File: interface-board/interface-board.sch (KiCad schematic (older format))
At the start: 21 parts, among them J1 HECS, J10 AUX, J11 UART, J12 NTC1, J13 NTC1, J16 Conn_01x23, J2 CASEFAN1, J3 CASEFAN2, J4 Bender-LV, J6 HV+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

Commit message: Getting there with layout of big board...
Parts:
- removed C2: 470uF, Capacitor_THT:CP_Radial_D10.0mm_P5.00mm, symbol Device:C
- removed F4: 20A, Fuse:Fuseholder_Cylinder-5x20mm_Schurter_0031_8201_Horizontal_Open, symbol Device:Fuse
- removed JP5: SolderJumper_2_Open, Jumper:SolderJumper-2_P1.3mm_Open_RoundedPad1.0x1.5mm, symbol Jumper:SolderJumper_2_Open
- removed JP6, JP7: SolderJumper_2_Bridged, Jumper:SolderJumper-2_P1.3mm_Bridged_RoundedPad1.0x1.5mm, symbol Jumper:SolderJumper_2_Bridged
- added F1: 2A, CustomFootprints:Fuseholder_Cylinder-5x20mm_Schurter_0031_8201_Horizontal_Open_3d, symbol Device:Fuse
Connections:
- wire segments 107 -> 104
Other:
- note added: "Return from safety loop"
- note added: "change to open jumpers"
- note removed: "Fuses?"

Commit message: Interface-board largely routed
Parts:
- removed J10: AUX, Connector_Wago:Wago_734-134_1x04_P3.50mm_Vertical, symbol Connector_Generic:Conn_01x02
- removed JP2, JP3: Jumper, Jumper:SolderJumper-2_P1.3mm_Open_RoundedPad1.0x1.5mm, symbol Jumper:SolderJumper_2_Open
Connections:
- net labels added: SCL, SDA
- wire segments 104 -> 100
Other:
- moved on the sheet: F1

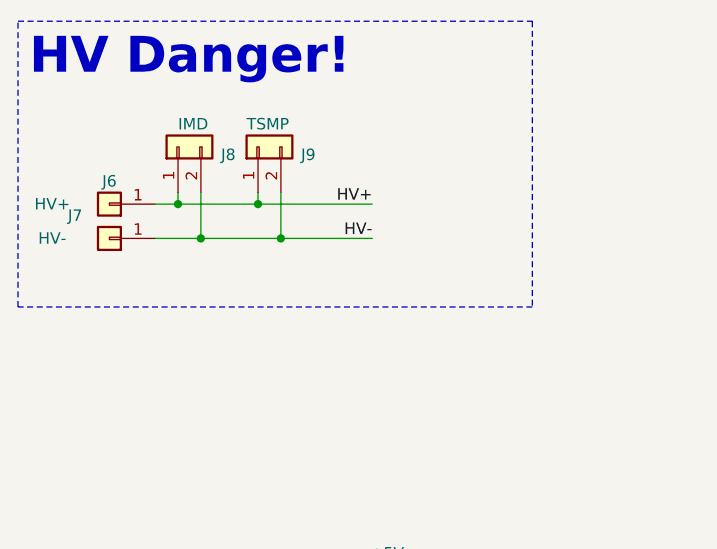
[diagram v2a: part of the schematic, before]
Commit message: Fully routed, added blinky DC/DC, added silkscreen labels, bumped 5V traces up to 0.025"
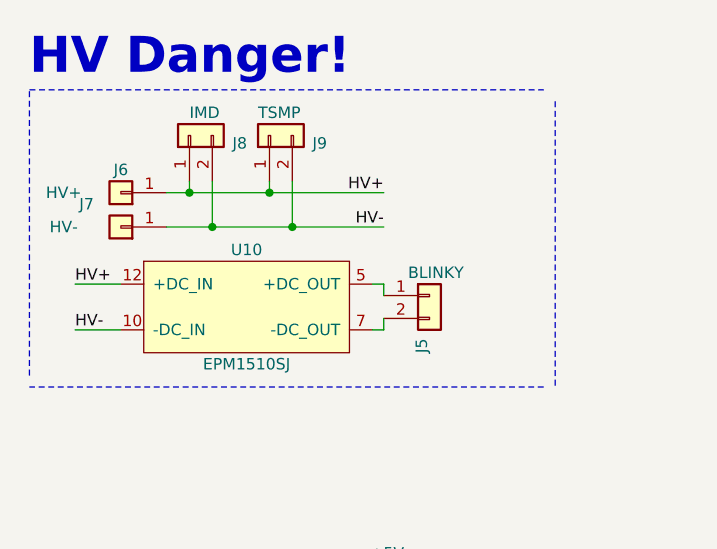
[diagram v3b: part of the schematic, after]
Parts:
- added J5: BLINKY, Connector_Phoenix_MC_HighVoltage:PhoenixContact_MCV_1,5_2-G-5.08_1x02_P5.08mm_Vertical, symbol Connector_Generic:Conn_01x02
- added U10: EPM1510SJ, CustomFootprints:EPM1510SJ, symbol CUSTOM_IC:EPM1510SJ
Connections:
- net HV+: now also U10.12 (+DC_IN)
- net HV-: now also U10.10 (-DC_IN)
- new net: J5.1 (Pin_1), U10.5 (+DC_OUT)
- new net: J5.2 (Pin_2), U10.7 (-DC_OUT)
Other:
- moved on the sheet: J6, J7, J8, J9
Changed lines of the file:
@@
 Comment4 ""
 $EndDescr
-Text Label 2100 1350 2    50   ~ 0
+Text Label 2150 1300 2    50   ~ 0
 HV+
-Text Label 2100 1500 2    50   ~ 0
+Text Label 2150 1450 2    50   ~ 0
 HV-
 Text Label 1350 6150 2    50   ~ 0
@@
 L Connector_Generic:Conn_01x01 J7
 U 1 1 5C7C388D
-P 950 1500
-F 0 "J7" H 1100 1400 50  0000 C CNN
-F 1 "HV-" H 1200 1500 50  0000 C CNN
-F 2 "MountingHole:MountingHole_4.3mm_M4_Pad_Via" H 950 1500 50  0001 C CNN
-F 3 "~" H 950 1500 50  0001 C CNN
-	1    950  1500
+P 1000 1450
+F 0 "J7" H 1150 1350 50  0000 C CNN
+F 1 "HV-" H 1250 1450 50  0000 C CNN
+F 2 "MountingHole:MountingHole_4.3mm_M4_Pad_Via" H 1000 1450 50  0001 C CNN
+F 3 "~" H 1000 1450 50  0001 C CNN
+	1    1000 1450
 	-1   0    0    1
 $EndComp
@@
 L Connector_Generic:Conn_01x01 J6
 U 1 1 5C83C6D2
-P 950 1350
-F 0 "J6" H 950 1250 50  0000 C CNN
-F 1 "HV+" H 1200 1350 50  0000 C CNN
-F 2 "MountingHole:MountingHole_4.3mm_M4_Pad_Via" H 950 1350 50  0001 C CNN
-F 3 "~" H 950 1350 50  0001 C CNN
-	1    950  1350
+P 1000 1300
+F 0 "J6" H 1000 1200 50  0000 C CNN
+F 1 "HV+" H 1250 1300 50  0000 C CNN
+F 2 "MountingHole:MountingHole_4.3mm_M4_Pad_Via" H 1000 1300 50  0001 C CNN
+F 3 "~" H 1000 1300 50  0001 C CNN
+	1    1000 1300
 	-1   0    0    1
 $EndComp
@@
 L Connector_Generic:Conn_01x02 J8
 U 1 1 5C871653
-P 1250 1100
-F 0 "J8" V 1216 912 50  0000 R CNN
-F 1 "IMD" V 1350 1100 50  0000 R CNN
-F 2 "Connector_Phoenix_MC_HighVoltage:PhoenixContact_MCV_1,5_2-G-5.08_1x02_P5.08mm_Vertical" H 1250 1100 50  0001 C CNN
-F 3 "~" H 1250 1100 50  0001 C CNN
-	1    1250 1100
+P 1300 1050
+F 0 "J8" V 1266 862 50  0000 R CNN
+F 1 "IMD" V 1400 1050 50  0000 R CNN
+F 2 "Connector_Phoenix_MC_HighVoltage:PhoenixContact_MCV_1,5_2-G-5.08_1x02_P5.08mm_Vertical" H 1300 1050 50  0001 C CNN
+F 3 "~" H 1300 1050 50  0001 C CNN
+	1    1300 1050
 	0    -1   -1   0
 $EndComp
 Wire Wire Line
-	1150 1350 1250 1350
-Wire Wire Line
-	1250 1300 1250 1350
-Wire Wire Line
-	1350 1300 1350 1500
-Wire Wire Line
-	1350 1500 1150 1500
-Connection ~ 1250 1350
+	1200 1300 1300 1300
+Wire Wire Line
+	1300 1250 1300 1300
+Wire Wire Line
+	1400 1250 1400 1450
+Wire Wire Line
+	1400 1450 1200 1450
+Connection ~ 1300 1300
 $Sheet
 S 4600 1150 1600 900
@@
 L Connector_Generic:Conn_01x02 J9
 U 1 1 5C4C2740
-P 1600 1100
-F 0 "J9" V 1566 912 50  0000 R CNN
-F 1 "TSMP" V 1700 1150 50  0000 R CNN
-F 2 "Connector_Phoenix_MC_HighVoltage:PhoenixContact_MCV_1,5_2-G-5.08_1x02_P5.08mm_Vertical" H 1600 1100 50  0001 C CNN
-F 3 "~" H 1600 1100 50  0001 C CNN
-	1    1600 1100
+P 1650 1050
+F 0 "J9" V 1616 862 50  0000 R CNN
+F 1 "TSMP" V 1750 1100 50  0000 R CNN
+F 2 "Connector_Phoenix_MC_HighVoltage:PhoenixContact_MCV_1,5_2-G-5.08_1x02_P5.08mm_Vertical" H 1650 1050 50  0001 C CNN
+F 3 "~" H 1650 1050 50  0001 C CNN
+	1    1650 1050
 	0    -1   -1   0
 $EndComp
 Wire Wire Line
-	1250 1350 1600 1350
-Wire Wire Line
-	1600 1300 1600 1350
-Connection ~ 1600 1350
-Wire Wire Line
-	1700 1300 1700 1500
-Wire Wire Line
-	1350 1500 1700 1500
-Connection ~ 1350 1500
+	1300 1300 1650 1300
+Wire Wire Line
+	1650 1250 1650 1300
+Connection ~ 1650 1300
+Wire Wire Line
+	1750 1250 1750 1450
+Wire Wire Line
+	1400 1450 1750 1450
+Connection ~ 1400 1450
 Text Label 3850 2550 0    50   ~ 0
 HV+
@@
 Text Label 4300 1350 0    50   ~ 0
 CAN-
-Connection ~ 1700 1500
+Connection ~ 1750 1450
 Text Label 6500 1800 2    50   ~ 0
 TEMP_1
@@
 $EndComp
 Wire Notes Line width 39 rgb(253, 0, 0)
-	550  550  2800 550
+	600  850  2850 850
 Wire Notes Line width 39 rgb(255, 0, 0)
-	2800 550  2800 1800
+	2900 900  2900 2150
 Wire Notes Line width 39 rgb(255, 0, 0)
-	2800 1800 550  1800
+	2850 2150 600  2150
 Wire Notes Line width 39 rgb(255, 0, 0)
-	550  1800 550  550
+	600  2100 600  850
 Text Notes 600  800  0    157  ~ 31
 HV Danger!
 Wire Wire Line
-	1600 1350 2100 1350
-Wire Wire Line
-	1700 1500 2100 1500
+	1650 1300 2150 1300
+Wire Wire Line
+	1750 1450 2150 1450
 $Comp
 L Connector_Generic:Conn_01x23 J16
@@
 Wire Wire Line
 	8850 2450 8950 2450
+$Comp
+L CUSTOM_IC:EPM1510SJ U10
+U 1 1 5C600D22
+P 1550 2000
+F 0 "U10" H 1550 2450 50  0000 C CNN
+F 1 "EPM1510SJ" H 1550 1950 50  0000 C CNN
+F 2 "CustomFootprints:EPM1510SJ" H 1550 2000 50  0001 C CNN
+F 3 "" H 1550 2000 50  0001 C CNN
+	1    1550 2000
+	1    0    0    -1
+$EndComp
+Wire Wire Line
+	1000 1700 800  1700
+Wire Wire Line
+	1000 1900 800  1900
+Text Label 800  1700 0    50   ~ 0
+HV+
+Text Label 800  1900 0    50   ~ 0
+HV-
+$Comp
+L Connector_Generic:Conn_01x02 J5
+U 1 1 5C61B783
+P 2350 1750
+F 0 "J5" V 2316 1562 50  0000 R CNN
+F 1 "BLINKY" H 2500 1850 50  0000 R CNN
+F 2 "Connector_Phoenix_MC_HighVoltage:PhoenixContact_MCV_1,5_2-G-5.08_1x02_P5.08mm_Vertical" H 2350 1750 50  0001 C CNN
+F 3 "~" H 2350 1750 50  0001 C CNN
+	1    2350 1750
+	1    0    0    -1
+$EndComp
+Wire Wire Line
+	2100 1700 2150 1700
+Wire Wire Line
+	2150 1700 2150 1750
+Wire Wire Line
+	2100 1900 2150 1900
+Wire Wire Line
+	2150 1900 2150 1850
 $EndSCHEMATC

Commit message: Cleaned up 3d models
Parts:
- removed J7: HV-, MountingHole:MountingHole_4.3mm_M4_Pad_Via, symbol Connector_Generic:Conn_01x01
- removed J8: IMD, Connector_Phoenix_MC_HighVoltage:PhoenixContact_MCV_1,5_2-G-5.08_1x02_P5.08mm_Vertical, symbol Connector_Generic:Conn_01x02
- removed J9: TSMP, Connector_Phoenix_MC_HighVoltage:PhoenixContact_MCV_1,5_2-G-5.08_1x02_P5.08mm_Vertical, symbol Connector_Generic:Conn_01x02
- added J7: HV-, Connector_TE-Connectivity:TE_MATE-N-LOK_1-770870-x_1x03_P4.14mm_Vertical, symbol Connector_Generic:Conn_01x03
- added J8: HV+, Connector_TE-Connectivity:TE_MATE-N-LOK_1-770870-x_1x03_P4.14mm_Vertical, symbol Connector_Generic:Conn_01x03
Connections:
- net HV+: now also J8.1 (Pin_1), J8.2 (Pin_2), J8.3 (Pin_3)
- net HV-: now also J7.1 (Pin_1), J7.2 (Pin_2), J7.3 (Pin_3)
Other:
- moved on the sheet: J6
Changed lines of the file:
@@
 Comment4 ""
 $EndDescr
-Text Label 2150 1300 2    50   ~ 0
+Text Label 2100 1150 2    50   ~ 0
 HV+
-Text Label 2150 1450 2    50   ~ 0
+Text Label 2100 1400 2    50   ~ 0
 HV-
 Text Label 1350 6150 2    50   ~ 0
@@
 CAN-
 $Comp
-L Connector_Generic:Conn_01x01 J7
-U 1 1 5C7C388D
-P 1000 1450
-F 0 "J7" H 1150 1350 50  0000 C CNN
-F 1 "HV-" H 1250 1450 50  0000 C CNN
-F 2 "MountingHole:MountingHole_4.3mm_M4_Pad_Via" H 1000 1450 50  0001 C CNN
-F 3 "~" H 1000 1450 50  0001 C CNN
-	1    1000 1450
-	-1   0    0    1
-$EndComp
-$Comp
 L Connector_Generic:Conn_01x01 J6
 U 1 1 5C83C6D2
-P 1000 1300
-F 0 "J6" H 1000 1200 50  0000 C CNN
-F 1 "HV+" H 1250 1300 50  0000 C CNN
-F 2 "MountingHole:MountingHole_4.3mm_M4_Pad_Via" H 1000 1300 50  0001 C CNN
-F 3 "~" H 1000 1300 50  0001 C CNN
-	1    1000 1300
+P 950 1150
+F 0 "J6" H 950 1050 50  0000 C CNN
+F 1 "HV+" H 1100 1150 50  0000 C CNN
+F 2 "MountingHole:MountingHole_4.3mm_M4_Pad_Via" H 950 1150 50  0001 C CNN
+F 3 "~" H 950 1150 50  0001 C CNN
+	1    950  1150
 	-1   0    0    1
 $EndComp
-$Comp
-L Connector_Generic:Conn_01x02 J8
-U 1 1 5C871653
-P 1300 1050
-F 0 "J8" V 1266 862 50  0000 R CNN
-F 1 "IMD" V 1400 1050 50  0000 R CNN
-F 2 "Connector_Phoenix_MC_HighVoltage:PhoenixContact_MCV_1,5_2-G-5.08_1x02_P5.08mm_Vertical" H 1300 1050 50  0001 C CNN
-F 3 "~" H 1300 1050 50  0001 C CNN
-	1    1300 1050
-	0    -1   -1   0
-$EndComp
-Wire Wire Line
-	1200 1300 1300 1300
-Wire Wire Line
-	1300 1250 1300 1300
-Wire Wire Line
-	1400 1250 1400 1450
-Wire Wire Line
-	1400 1450 1200 1450
-Connection ~ 1300 1300
 $Sheet
 S 4600 1150 1600 900
@@
 Text Notes 8150 2250 0    50   ~ 0
 Global nets connected to this sheet: \nGND, 5V
-$Comp
-L Connector_Generic:Conn_01x02 J9
-U 1 1 5C4C2740
-P 1650 1050
-F 0 "J9" V 1616 862 50  0000 R CNN
-F 1 "TSMP" V 1750 1100 50  0000 R CNN
-F 2 "Connector_Phoenix_MC_HighVoltage:PhoenixContact_MCV_1,5_2-G-5.08_1x02_P5.08mm_Vertical" H 1650 1050 50  0001 C CNN
-F 3 "~" H 1650 1050 50  0001 C CNN
-	1    1650 1050
-	0    -1   -1   0
-$EndComp
-Wire Wire Line
-	1300 1300 1650 1300
-Wire Wire Line
-	1650 1250 1650 1300
-Connection ~ 1650 1300
-Wire Wire Line
-	1750 1250 1750 1450
-Wire Wire Line
-	1400 1450 1750 1450
-Connection ~ 1400 1450
 Text Label 3850 2550 0    50   ~ 0
 HV+
@@
 Text Label 4300 1350 0    50   ~ 0
 CAN-
-Connection ~ 1750 1450
 Text Label 6500 1800 2    50   ~ 0
 TEMP_1
@@
 Text Notes 600  800  0    157  ~ 31
 HV Danger!
-Wire Wire Line
-	1650 1300 2150 1300
-Wire Wire Line
-	1750 1450 2150 1450
 $Comp
 L Connector_Generic:Conn_01x23 J16
@@
 Wire Wire Line
 	2150 1900 2150 1850
+$Comp
+L Connector_Generic:Conn_01x03 J8
+U 1 1 5C622267
+P 1450 950
+F 0 "J8" V 1416 762 50  0000 R CNN
+F 1 "HV+" V 1325 762 50  0000 R CNN
+F 2 "Connector_TE-Connectivity:TE_MATE-N-LOK_1-770870-x_1x03_P4.14mm_Vertical" H 1450 950 50  0001 C CNN
+F 3 "~" H 1450 950 50  0001 C CNN
+	1    1450 950
+	0    -1   -1   0
+$EndComp
+Wire Wire Line
+	1150 1150 1350 1150
+Wire Wire Line
+	1150 1400 2100 1400
+Wire Wire Line
+	1550 1150 2100 1150
+Wire Wire Line
+	1350 1150 1450 1150
+Connection ~ 1350 1150
+Connection ~ 1550 1150
+Connection ~ 1450 1150
+Wire Wire Line
+	1450 1150 1550 1150
+$Comp
+L Connector_Generic:Conn_01x03 J7
+U 1 1 5C62A13D
+P 950 1400
+F 0 "J7" H 870 1075 50  0000 C CNN
+F 1 "HV-" H 1100 1400 50  0000 C CNN
+F 2 "Connector_TE-Connectivity:TE_MATE-N-LOK_1-770870-x_1x03_P4.14mm_Vertical" H 950 1400 50  0001 C CNN
+F 3 "~" H 950 1400 50  0001 C CNN
+	1    950  1400
+	-1   0    0    1
+$EndComp
+Wire Wire Line
+	1150 1300 1150 1400
+Connection ~ 1150 1400
+Wire Wire Line
+	1150 1400 1150 1500
 $EndSCHEMATC

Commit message: Put Vicor on a removable module
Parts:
- added C?: 0.1uF, Capacitor_SMD:C_0603_1608Metric, symbol Device:C
- added C? (x2): 10uF, Capacitor_SMD:C_0603_1608Metric, symbol Device:C
- added U?: R-78E5.0-0.5, Converter_DCDC:Converter_DCDC_RECOM_R-78E-0.5_THT, symbol Regulator_Switching:R-78E5.0-0.5
- U10: symbol CUSTOM_IC:EPM1510SJ -> interface-board-rescue:EPM1510SJ-CUSTOM_IC
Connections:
- net GND: now also C?.2, C?.2, C?.2, U?.2 (GND)
- net DC->DC Converters/HV+ renamed DC->DC Converter/HV+
- new net 12V_IN: C?.1, U?.1 (IN)
- new net 5V_OUT: C?.1, C?.1, U?.3 (OUT)
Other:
- note added: "12V->5V"
- note added: "Can remove this"
- note added: "Current monitor for HV and UART debug port"
- note added: "Local fan controls and thermocoupler inputs"
- note added: "SHDN_LOOP_OUT is connected to 12V through shutdown loop"
- note added: "This is to run a HV indicator LED (called blinky)."
- note removed: "change to open jumpers"
- moved on the sheet: C1, F1, J4
